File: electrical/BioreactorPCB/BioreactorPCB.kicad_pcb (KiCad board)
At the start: 2 copper layers, 81.5 x 84.9 mm, 77 parts, among them IC1 AL5809-20P1-7, IC2 VEML7700-TR, J1 61300311121, J10 USB_B, J11 Conn_01x06_Male, J12 Conn_02x03_Odd_Even, J13 PJ-202A, J14 Conn_01x05_Male, J2 61300311121, J3 Conn_01x05_Male, J4 Conn_01x06_Male, J5 OSTTC022162, J6 OSTTC022162, J7 OSTTC042162, J8 OSTTC042162, J9 OSTTC042162, Q1 2N3905, Q2 IRF540N, Q3 FQP47P06, Q4 TL2575HV-05IKV, U1 L293D, U2 FT232RL, U3 ATMEGA328P-AUR, U4 TCA39306DCUR, Y1 16 mHz

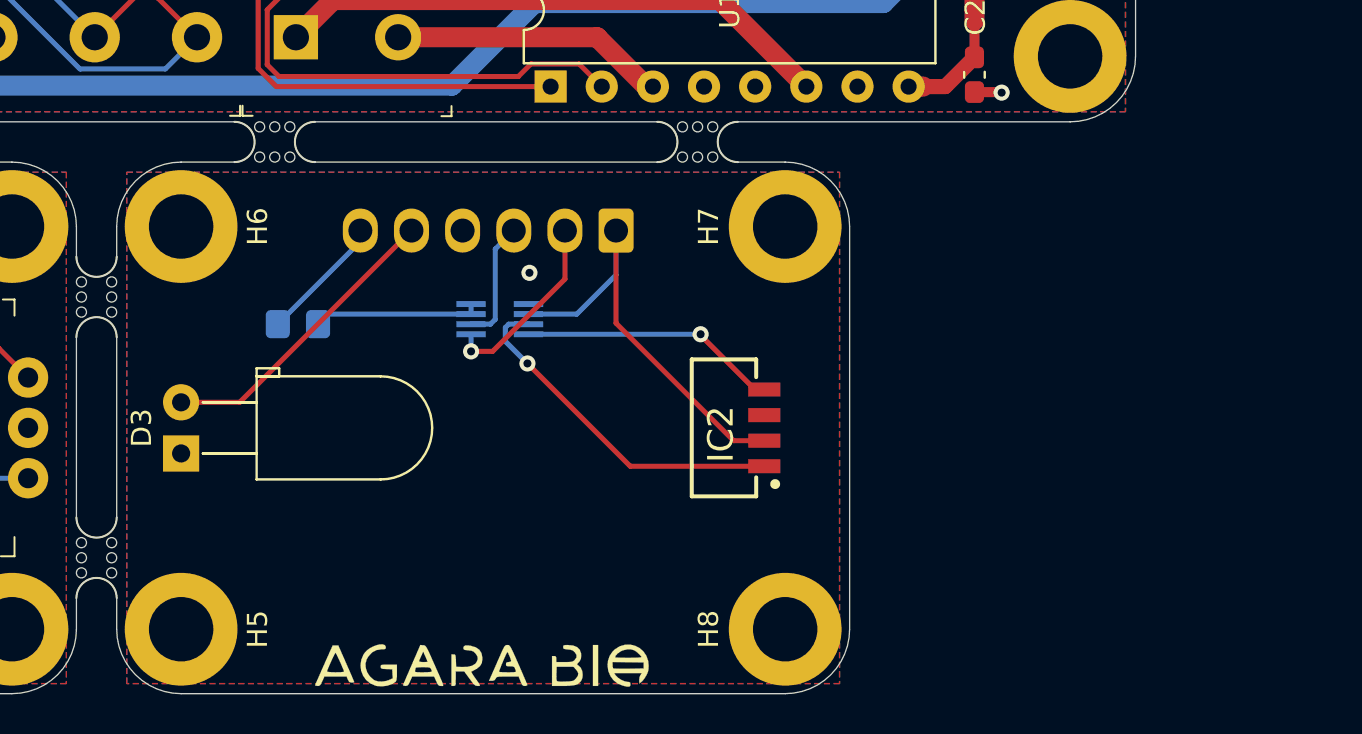
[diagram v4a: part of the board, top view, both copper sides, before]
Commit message: changed layout and schematic to reflect addition of a third daughterboard and separation of the LED and photodiode onto separate boards
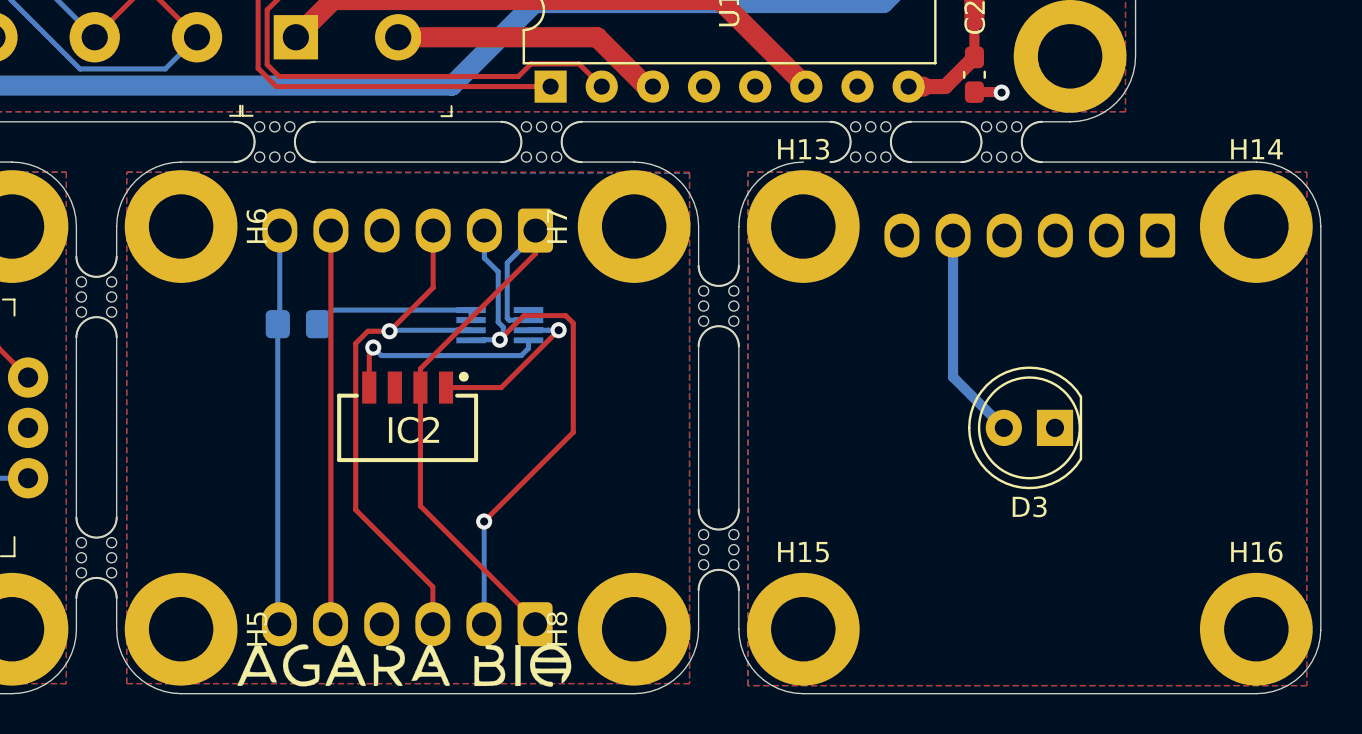
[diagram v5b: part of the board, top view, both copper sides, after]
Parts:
- added H13: MountingHole_Pad, MountingHole:MountingHole_3.2mm_M3_DIN965_Pad, F.Cu at (146.8, 99.2)
- added H14: MountingHole_Pad, MountingHole:MountingHole_3.2mm_M3_DIN965_Pad, F.Cu at (169.2, 99.2)
- added H15: MountingHole_Pad, MountingHole:MountingHole_3.2mm_M3_DIN965_Pad, F.Cu at (146.8, 119.2)
- added H16: MountingHole_Pad, MountingHole:MountingHole_3.2mm_M3_DIN965_Pad, F.Cu at (169.2, 119.2)
- added J15: Conn_01x06_Male, Connector_Molex:Molex_KK-254_AE-6410-06A_1x06_P2.54mm_Vertical, B.Cu at (133.4, 119.0)
- added J16: Conn_01x06_Male, Connector_Molex:Molex_KK-254_AE-6410-06A_1x06_P2.54mm_Vertical, B.Cu at (164.3, 99.7)
- added mouse-bite-2mm-slot: VAL**, Panelization:mouse-bite-2mm-slot, F.Cu at (156.6, 95.0)
- added mouse-bite-2mm-slot: VAL**, Panelization:mouse-bite-2mm-slot, F.Cu at (150.1, 95.0)
- added mouse-bite-2mm-slot: VAL**, Panelization:mouse-bite-2mm-slot, F.Cu at (142.6, 115.2)
- added mouse-bite-2mm-slot: VAL**, Panelization:mouse-bite-2mm-slot, F.Cu at (142.6, 103.2)
- D3: footprint LED_THT:LED_D5.0mm_Horizontal_O3.81mm_Z9.0mm -> LED_THT:LED_D5.0mm
- moved D3 43.4 mm to (159.2, 109.2), turned to 180 degrees
- moved IC2 14.8 mm to (130.5, 107.6), turned to 180 degrees
- moved mouse-bite-2mm-slot 7.75 mm to (133.8, 95.0)
- moved H7 7.50 mm to (138.3, 99.2)
- moved H8 7.50 mm to (138.3, 119.2)
- moved J11 4.00 mm to (133.4, 99.4)
- moved G*** 3.85 mm to (127.0, 121.0)
- moved U4 0.30 mm to (131.7, 104.1)
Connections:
- D3 pad 1: GND2 -> GND4
- J11 pad 5: Net-(D3-Pad2) -> PHOTO_LED
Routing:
- net SCL2: track 6.09 -> 27.4 mm, vias 0 -> 1
- net PHOTO_LED: track 0.00 -> 19.6 mm
- net SDA2: track 9.41 -> 28.4 mm, vias 1 -> 2
- net 5V_3: track 6.35 -> 19.6 mm
- net SCL1: track 17.3 -> 8.27 mm
- net 3V3_2: track 21.7 -> 30.3 mm
- net Net-(D3-Pad2): track 15.0 -> 10.6 mm
- net SDA1: track 12.9 -> 10.5 mm
- net Net-(R8-Pad2): track 8.31 -> 9.10 mm
- net GND2: vias 1 -> 0
- added copper zone on B.Cu, net GND4
- added copper zone on F.Cu, net GND4
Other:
- board size 81.5 x 84.9 mm -> 90.7 x 84.9 mm

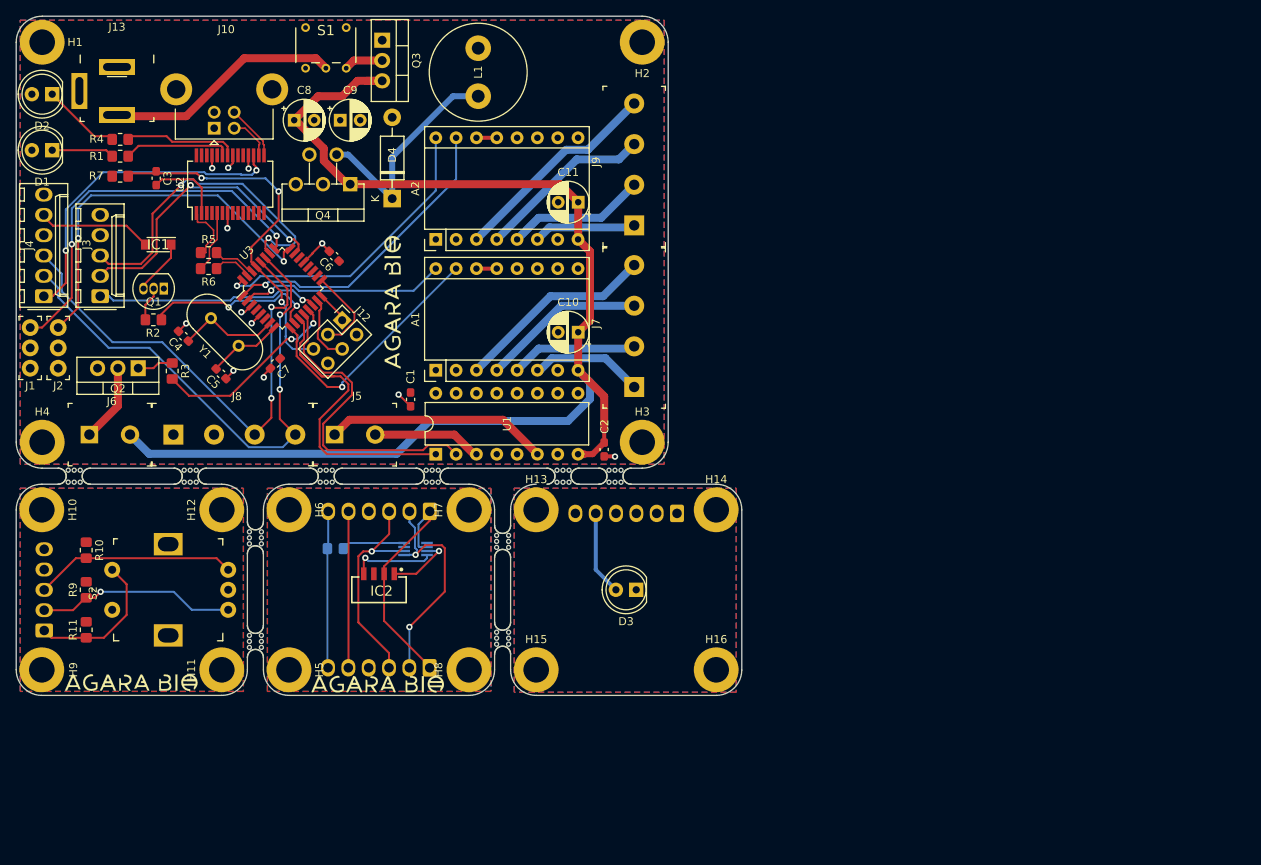
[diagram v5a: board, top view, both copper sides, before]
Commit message: Added 10K pullups on the i2c SDA and SCL. Apparently AVR internal pullups are too weak! Oops.
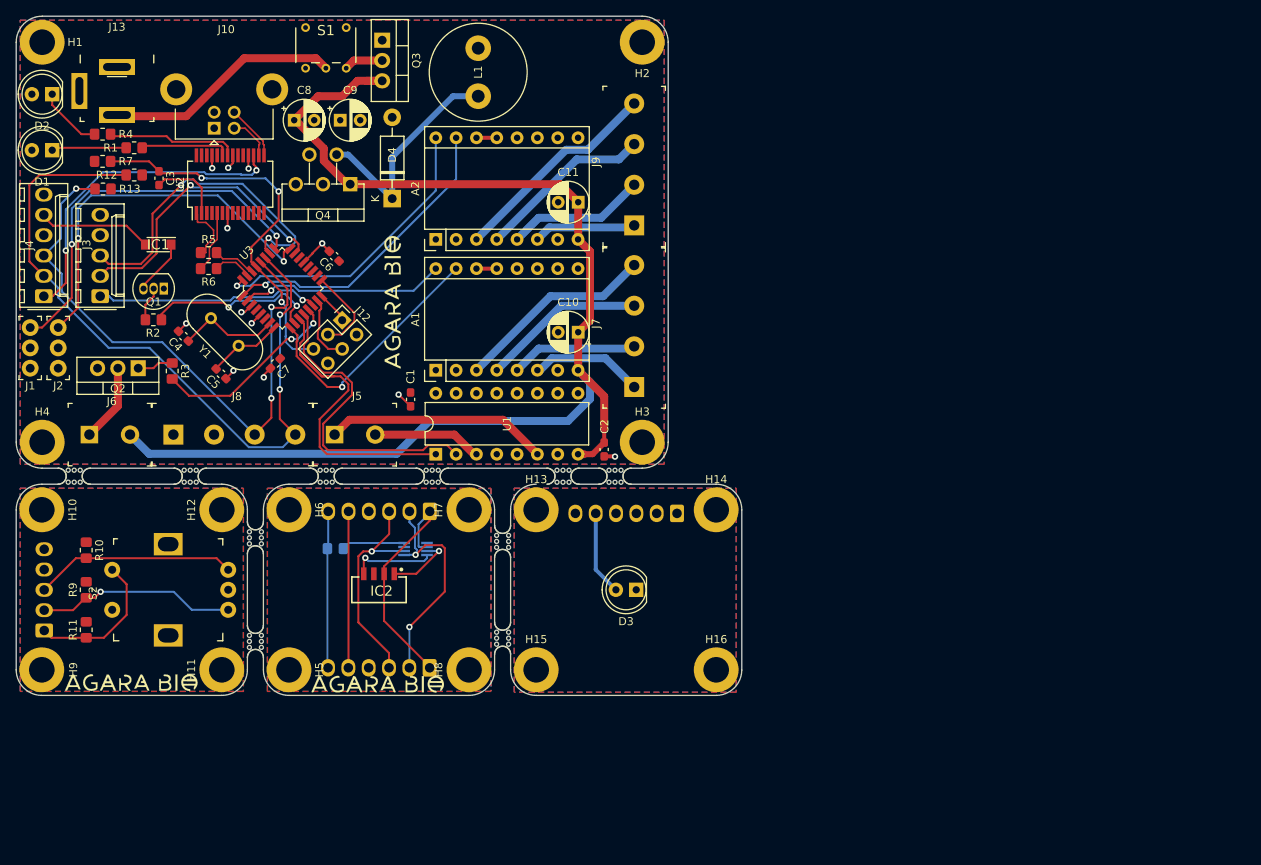
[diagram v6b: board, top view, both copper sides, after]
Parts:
- added R12: 10K, Resistor_SMD:R_0805_2012Metric_Pad1.20x1.40mm_HandSolder, F.Cu at (96.5, 57.4)
- added R13: 10K, Resistor_SMD:R_0805_2012Metric_Pad1.20x1.40mm_HandSolder, F.Cu at (92.6, 59.1)
- moved R7 2.87 mm to (92.5, 55.6)
- moved R4 2.29 mm to (92.5, 52.2)
- moved R1 2.04 mm to (96.5, 54.0)
- moved C3 0.35 mm to (99.6, 57.8)
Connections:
- A1 pad 10: (no net) -> unconnected-(A1-Pad10)
- A1 pad 11: (no net) -> unconnected-(A1-Pad11)
- A1 pad 12: (no net) -> unconnected-(A1-Pad12)
- A1 pad 9: (no net) -> unconnected-(A1-Pad9)
- A2 pad 10: (no net) -> unconnected-(A2-Pad10)
- A2 pad 11: (no net) -> unconnected-(A2-Pad11)
- A2 pad 12: (no net) -> unconnected-(A2-Pad12)
- A2 pad 9: (no net) -> unconnected-(A2-Pad9)
- J10 pad 1: (no net) -> unconnected-(J10-Pad1)
- J16 pad 1: (no net) -> unconnected-(J16-Pad1)
- J16 pad 2: (no net) -> unconnected-(J16-Pad2)
- J16 pad 3: (no net) -> unconnected-(J16-Pad3)
- J16 pad 6: (no net) -> unconnected-(J16-Pad6)
- S1 pad 6: (no net) -> unconnected-(S1-Pad6)
- U1 pad 10: (no net) -> unconnected-(U1-Pad10)
- U1 pad 11: (no net) -> unconnected-(U1-Pad11)
- U1 pad 14: (no net) -> unconnected-(U1-Pad14)
- U1 pad 15: (no net) -> unconnected-(U1-Pad15)
- U1 pad 9: (no net) -> unconnected-(U1-Pad9)
- U2 pad 10: (no net) -> unconnected-(U2-Pad10)
- U2 pad 11: (no net) -> unconnected-(U2-Pad11)
- U2 pad 12: (no net) -> unconnected-(U2-Pad12)
- U2 pad 13: (no net) -> unconnected-(U2-Pad13)
- U2 pad 14: (no net) -> unconnected-(U2-Pad14)
- U2 pad 19: (no net) -> unconnected-(U2-Pad19)
- U2 pad 26: (no net) -> unconnected-(U2-Pad26)
- U2 pad 27: (no net) -> unconnected-(U2-Pad27)
- U2 pad 28: (no net) -> unconnected-(U2-Pad28)
- U2 pad 3: (no net) -> unconnected-(U2-Pad3)
- U2 pad 6: (no net) -> unconnected-(U2-Pad6)
- U2 pad 9: (no net) -> unconnected-(U2-Pad9)
- U3 pad 19: (no net) -> unconnected-(U3-Pad19)
- U3 pad 22: (no net) -> unconnected-(U3-Pad22)
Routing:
- net SDA: track 67.5 -> 92.3 mm
- net SCL: track 62.7 -> 75.1 mm, vias 2 -> 3
- net RESET: track 46.0 -> 48.5 mm
- net Net-(R4-Pad1): track 14.1 -> 16.4 mm
- net Net-(R1-Pad2): track 13.4 -> 11.6 mm
- net Net-(D1-Pad1): track 8.38 -> 9.94 mm
- net Net-(D2-Pad1): track 9.67 -> 8.16 mm
- net TEMP_OUT: track 49.1 -> 48.4 mm
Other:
- net class Default removed

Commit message: cleanup of tracks and plane
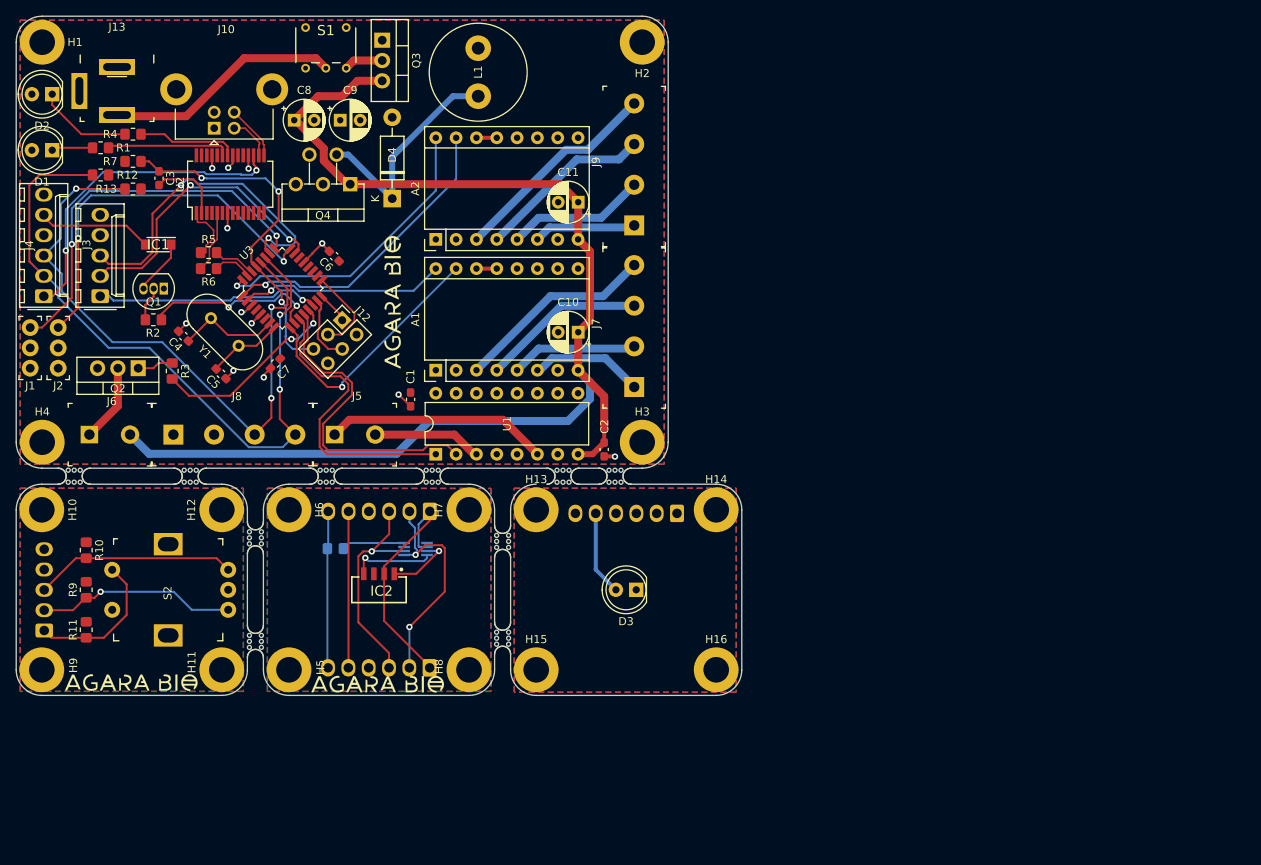
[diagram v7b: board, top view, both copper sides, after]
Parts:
- moved R1 4.20 mm to (92.3, 54.0)
- moved R12 4.20 mm to (92.3, 57.4)
- moved R4 3.80 mm to (96.3, 52.2)
- moved R7 3.80 mm to (96.3, 55.6)
- moved R13 3.75 mm to (96.3, 59.1)
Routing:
- net D7: track 42.8 -> 36.7 mm
- net SDA: track 92.3 -> 86.9 mm
- net Net-(D1-Pad1): track 9.94 -> 4.75 mm
- net RESET: track 48.5 -> 44.6 mm
- net Net-(R4-Pad1): track 16.4 -> 12.6 mm
- net Net-(D2-Pad1): track 8.16 -> 12.0 mm
- net SCL: track 75.1 -> 78.8 mm
- net Net-(R1-Pad2): track 11.6 -> 15.1 mm
- net +12V: track 158.5 -> 155.2 mm
- net RX_TX_N: track 6.27 -> 4.73 mm
- net Net-(IC1-Pad1): track 7.26 -> 6.51 mm
- net Net-(R8-Pad2): track 9.10 -> 8.39 mm
- net Net-(A2-Pad6): track 13.2 -> 12.5 mm
- net D4: track 26.5 -> 25.8 mm
- net D6: track 23.2 -> 22.5 mm
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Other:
- outline, holes or cut-outs redrawn

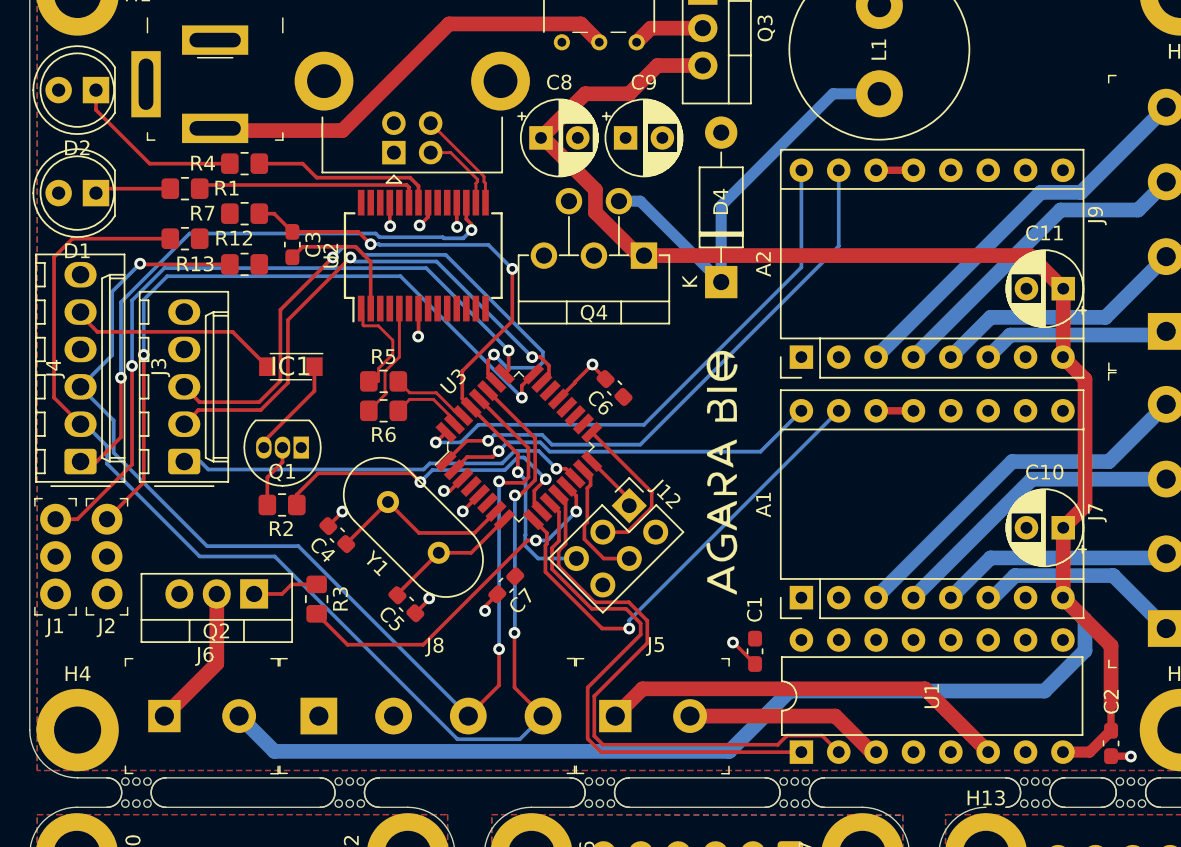
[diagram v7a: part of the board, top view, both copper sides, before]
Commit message: Added alternate Atmega328PB 32QFN package and rerouted board to match
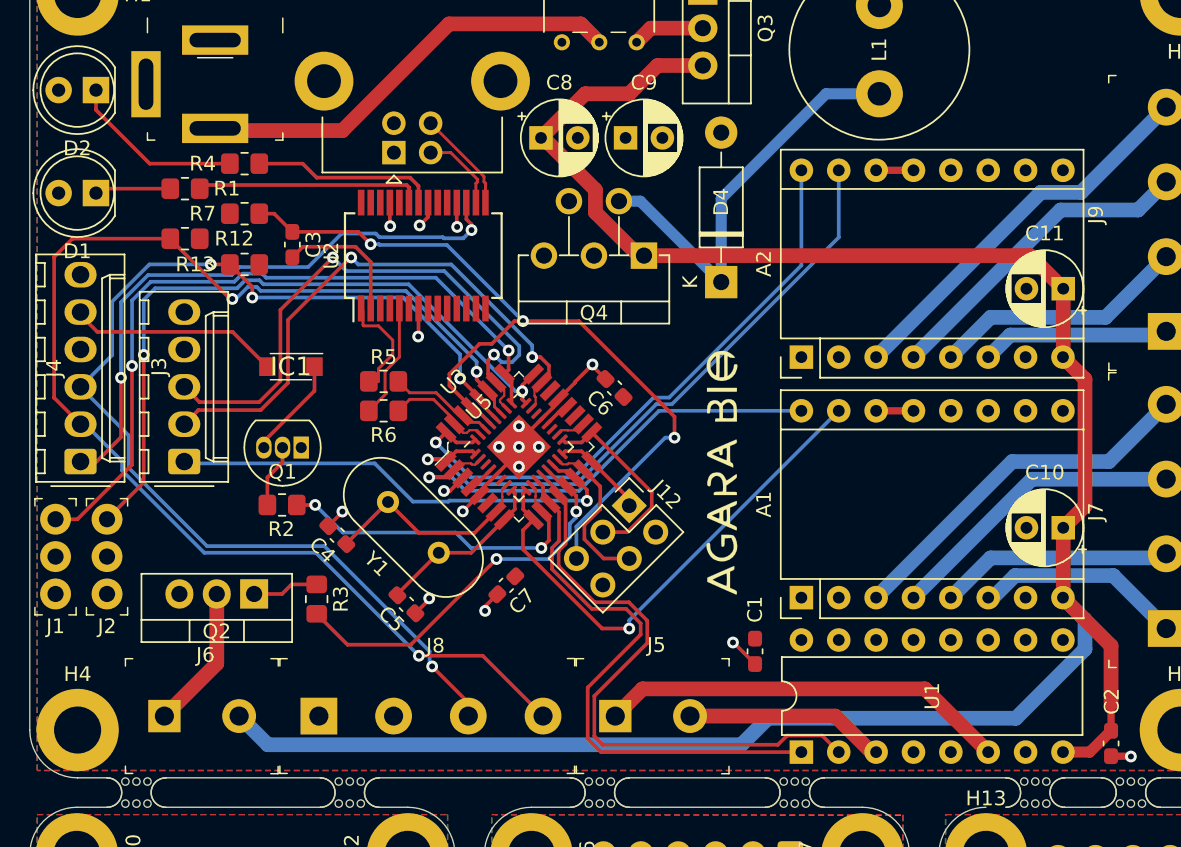
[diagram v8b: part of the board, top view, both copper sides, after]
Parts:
- added U5: ATmega328PB-M, Package_DFN_QFN:QFN-32-1EP_5x5mm_P0.5mm_EP3.1x3.1mm, F.Cu at (115.0, 71.5)
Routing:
- net RESET: track 44.6 -> 57.9 mm
- net GND: track 22.6 -> 29.5 mm, vias 12 -> 17
- net D3: track 38.5 -> 43.8 mm
- net D4: track 25.8 -> 30.7 mm
- net +5V: track 0.00 -> 4.69 mm
- net D2: track 37.4 -> 41.6 mm
- net BUTTON: track 28.1 -> 32.2 mm
- net D5: track 32.0 -> 34.8 mm
- net ROT_A: track 36.4 -> 39.0 mm
- net D9: track 24.2 -> 26.6 mm
- net XTAL-: track 9.37 -> 11.7 mm
- net MISO: track 3.61 -> 5.96 mm
- net SCK: track 10.8 -> 13.2 mm
- net SCL: track 78.8 -> 76.5 mm, vias 3 -> 4
- net RX_TX_N: track 4.73 -> 6.95 mm
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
